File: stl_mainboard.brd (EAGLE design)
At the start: 148.9 x 80 mm, 47 parts, among them IC1 LM555D, IC2 4017D, IC3 ULN2001AD, Q1 AUIRFR5305, Q2 AUIRFR5305, Q3 AUIRFR5305, Q4 AUIRFR5305, Q5 AUIRFR5305, Q6 AUIRFR5305, Q7 AUIRFR5305

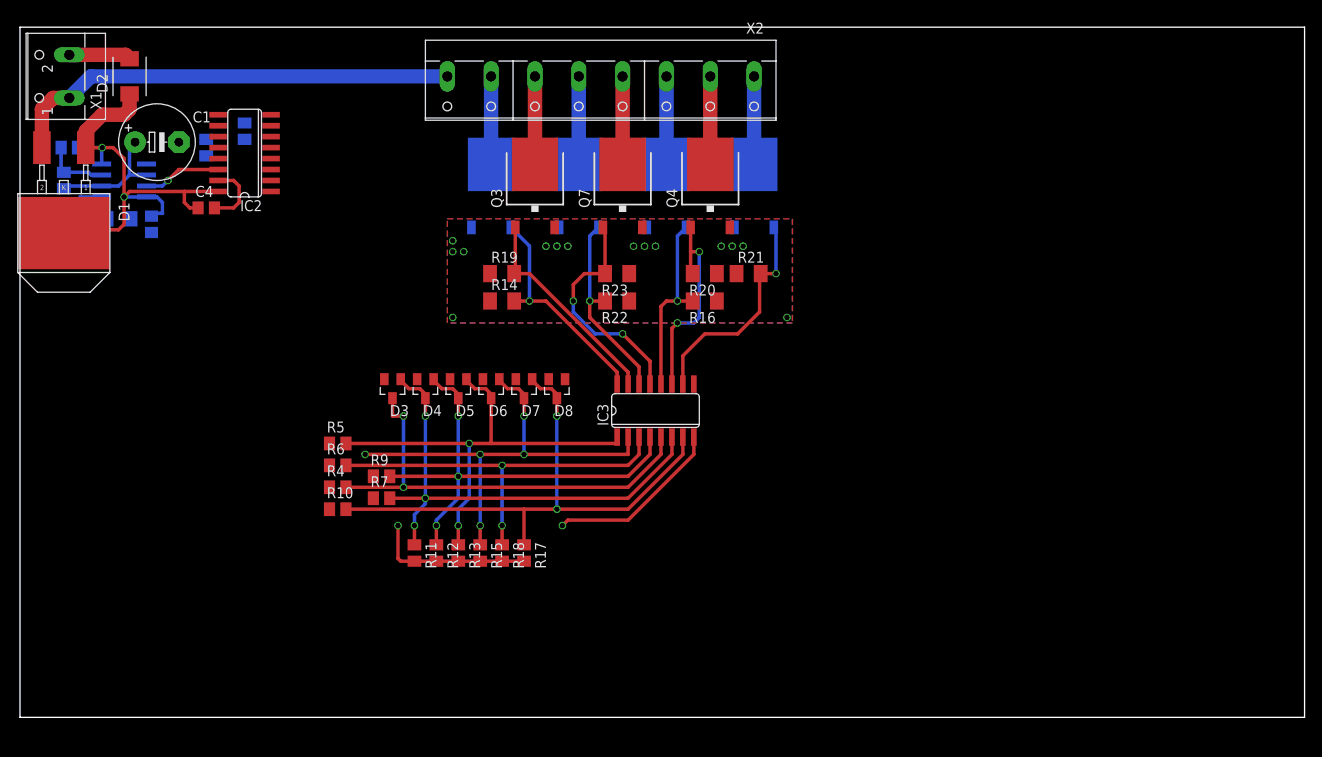
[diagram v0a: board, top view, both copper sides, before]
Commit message: board and schematics done
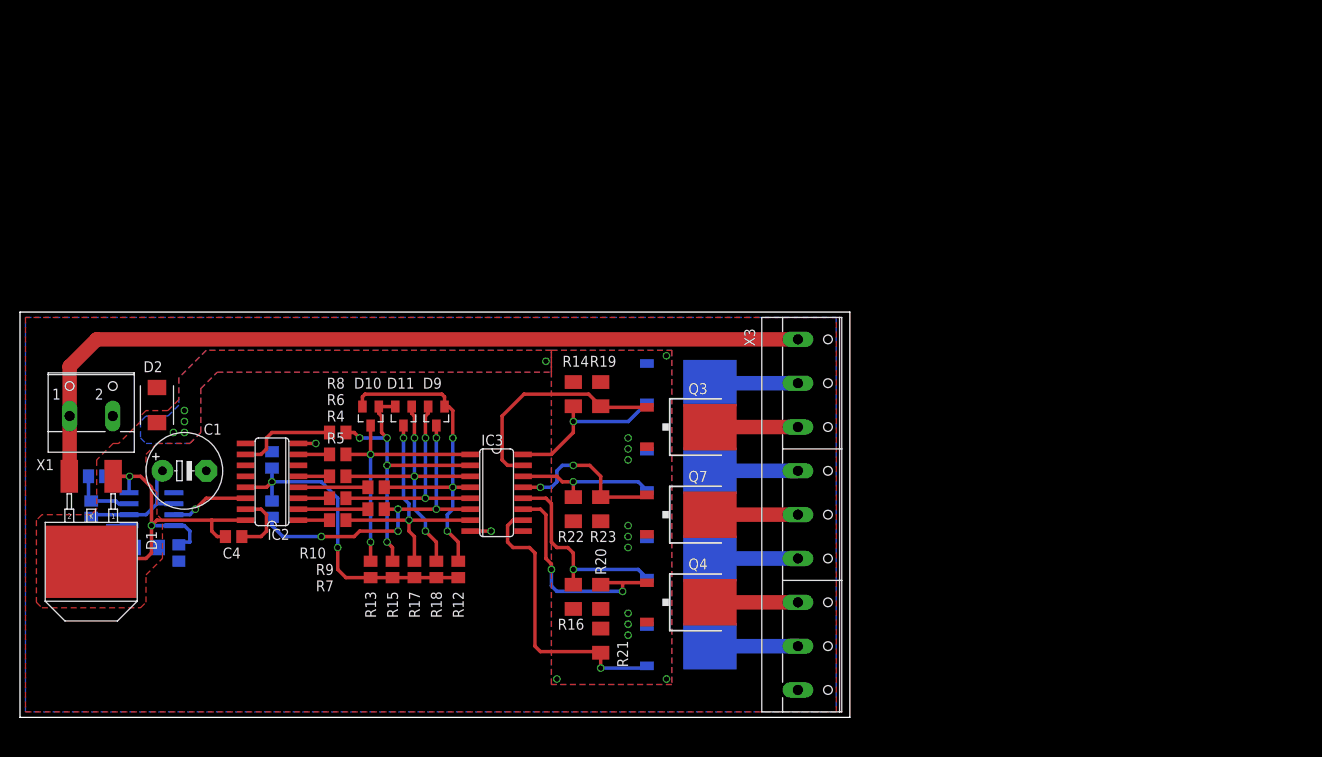
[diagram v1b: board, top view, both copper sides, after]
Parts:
- removed D3, D4, D5, D6, D7, D8: BAS40, diode:SOT23
- removed X2: (no value), con-wago-508:W237-8P
- added D10, D11, D9: BAS40-04, diode:SOT23
- added X3: (no value), con-wago-508:W237-9P
- moved Q5 53.9 mm to (77.5, 8.26), turned to 90 degrees
- moved Q4 48.3 mm to (77.5, 13.3), turned to 270 degrees
- moved R21 45.9 mm to (67.3, 8.89), turned to 270 degrees
- moved Q2 43.3 mm to (77.5, 18.4), turned to 90 degrees
- moved R20 39.4 mm to (67.3, 14.0), turned to 90 degrees
- moved Q7 38.9 mm to (77.5, 23.5), turned to 270 degrees
- moved X1 38.3 mm to (8.26, 36.2), turned to 0 degrees
- moved D1 38.2 mm to (8.26, 27.9)
- moved R2 38.2 mm to (8.89, 27.9)
- moved C4 38.2 mm to (24.8, 21.0)
- moved D2 38.2 mm to (15.9, 36.2)
- moved IC2 38.2 mm to (29.2, 27.3)
- moved C1 38.2 mm to (19.1, 28.6)
- moved C2 38.2 mm to (14.6, 19.7)
- moved C3 38.2 mm to (18.4, 19.1)
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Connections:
- removed net +12V: D1.2, X1.1, X2.8
- new net B+: D1.2, X1.1, X3.1
- net BULB2: now also X3.2; no longer X2.7
- net BULB3: now also X3.3; no longer X2.6
- net BULB4: now also X3.4; no longer X2.5
- net BULB5: now also X3.5; no longer X2.4
- net BULB6: now also X3.6; no longer X2.3
- net BULB7: now also X3.7; no longer X2.2
- net BULB8: now also X3.8; no longer X2.1
- net Q0: now also D9.2; no longer D3.3
- net Q1: now also D9.3; no longer D3.1, D4.3
- net Q2: now also D10.2, D9.1; no longer D4.1, D5.3
- net Q3: now also D10.3; no longer D5.1, D6.3
- net Q4: now also D10.1, D11.2; no longer D6.1, D7.3
- net Q5: now also D11.3; no longer D7.1, D8.3
- net Q6: now also D11.1; no longer D8.1
- net VSS: now also X3.9
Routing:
- net B+: track 0.00 -> 99.1 mm
- net +12V: track 53.0 -> 0.00 mm
- net Q5: track 64.8 -> 30.6 mm
- net Q0: track 51.7 -> 25.1 mm
- net Q3: track 53.8 -> 30.1 mm
- net VSS: track 35.6 -> 12.2 mm, vias 1 -> 2
- net Q1: track 58.5 -> 38.5 mm, vias 3 -> 5
- net CNTR_STOP: track 18.5 -> 38.2 mm, vias 1 -> 2
- net Q4: track 53.6 -> 35.2 mm, vias 5 -> 4
- net Q2: track 55.4 -> 41.4 mm
- net Q6: track 45.7 -> 33.5 mm, vias 2 -> 3
- net N$8: track 0.00 -> 11.5 mm
- net VDD: track 56.3 -> 46.4 mm, vias 16 -> 19
- net N$6: track 0.00 -> 8.04 mm
- net N$5: track 0.00 -> 8.04 mm
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- added copper zone on layer 1, net VSS
- added copper zone on layer 16, net VSS
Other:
- board size 148.9 x 80 mm -> 96.2 x 47 mm

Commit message: improve routing power polygones
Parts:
- moved C2 5.12 mm to (17.1, 15.2)
- moved C3 1.27 mm to (19.7, 19.1)
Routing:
- net VDD: track 46.4 -> 36.4 mm, vias 19 -> 21
- net N$1: track 7.32 -> 14.3 mm
- net B+: track 99.1 -> 99.8 mm
- net VSS: vias 2 -> 6

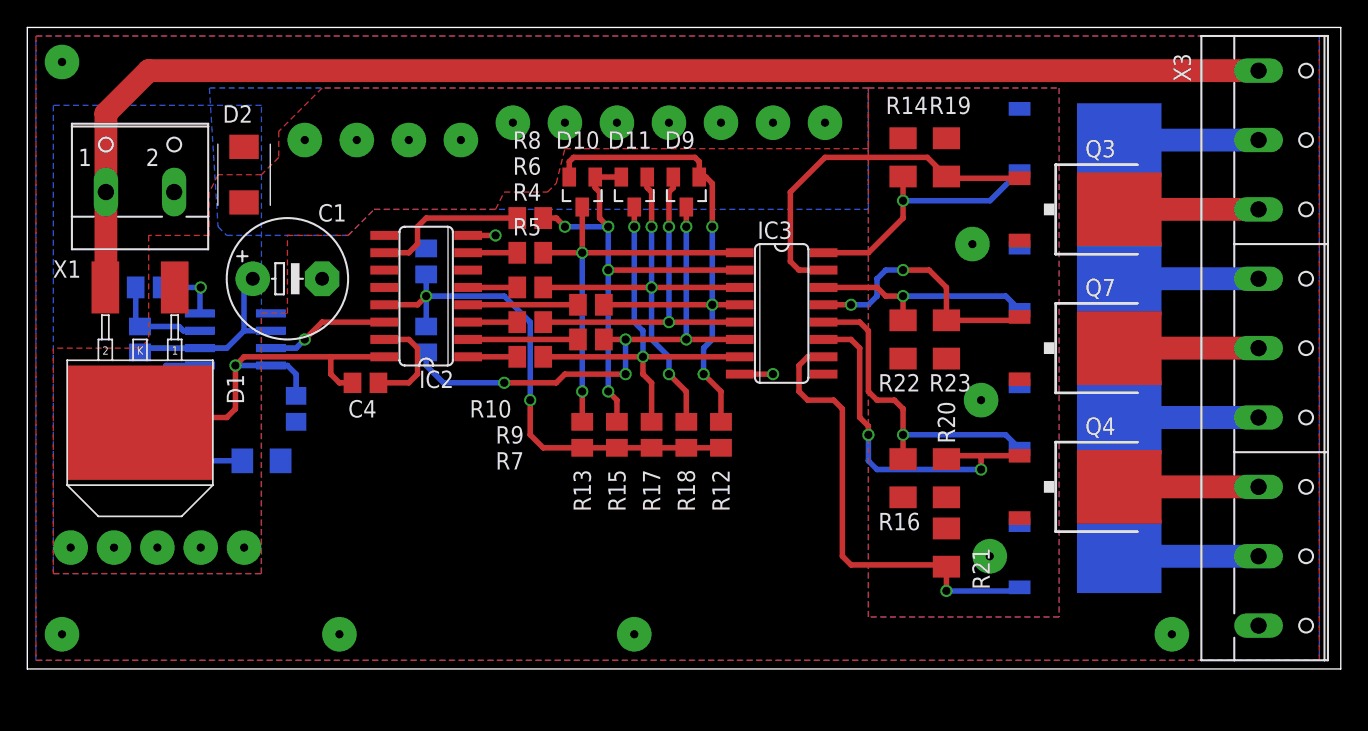
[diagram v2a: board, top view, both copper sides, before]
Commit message: No more 555 and 4017. STM8 instead.
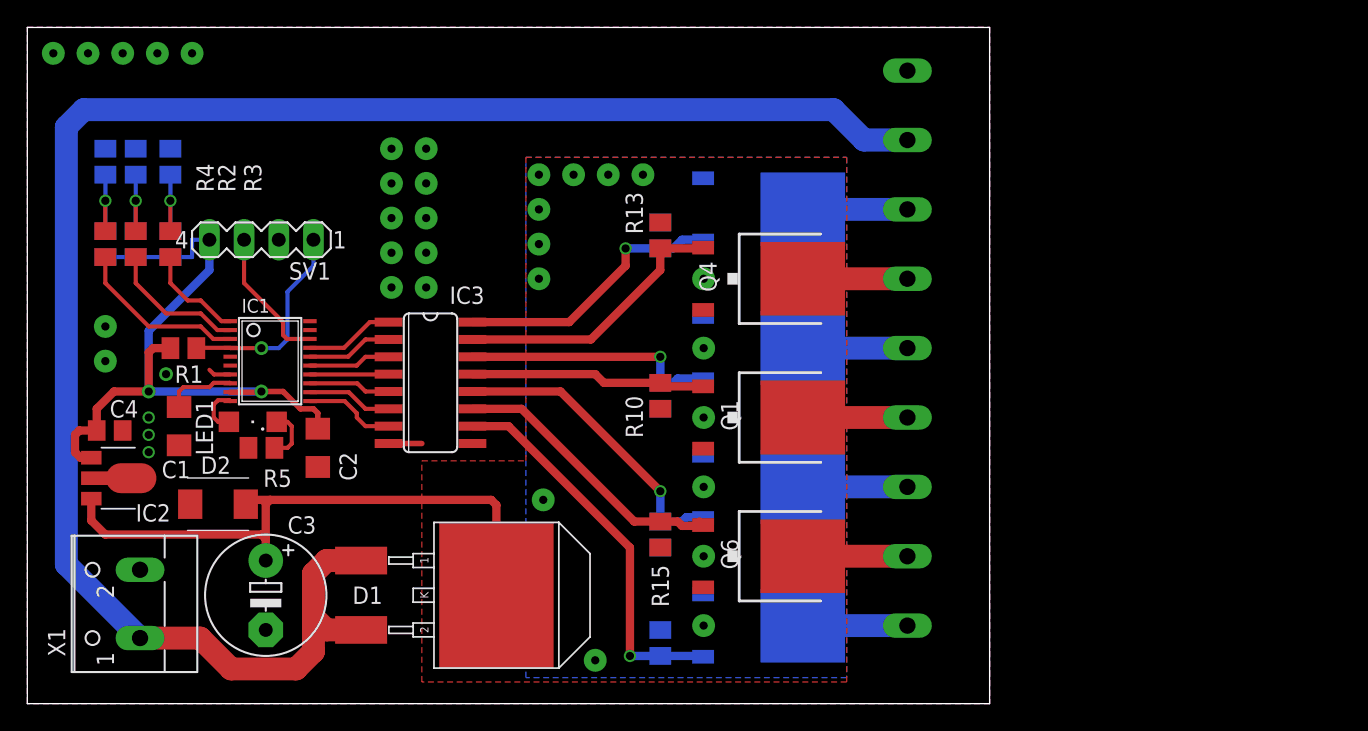
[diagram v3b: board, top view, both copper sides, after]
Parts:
- removed D10, D11, D9: BAS40-04, diode:SOT23
- removed R19, R20, R21, R22, R23: 1K, rcl:M1206
- removed X3: (no value), con-wago-508:W237-9P
- added LED1: (no value), led:SML1206
- added SV1: (no value), con-lstb:MA04-1
- added X2: (no value), con-wago-508:W237-9P
- C1: value 47 -> 1uF; device rcl:E5-8,5 -> rcl:C1206
- C2: value 0.01 -> 100nf
- C3: value 0.1uF -> 0.33; device rcl:C0805 -> rcl:E5-8,5
- C4: value 0.1uF -> 0.1
- D1: value 48CTQ060S -> 48CTQ060; device diode:TO263AB -> 48ctq060:TO263AB
- IC1: value LM555D -> STM8S003F3; device linear:SO08 -> stm8:TSSOP20
- IC2: value 4017D -> 78L05F; device 40xx:SO16 -> linear:SOT89
- R10, R11, R12, R13, R15, R4: value 0 -> 1K
- R14, R16: device rcl:M1206 -> rcl:M0805
- R3: value 4K2 -> 1K
- R5: value 0 -> 5k6
- moved R18 44.8 mm to (5.71, 31.1), flipped to the bottom
- moved R17 40.3 mm to (7.94, 31.1), flipped to the bottom
- moved R7 35.8 mm to (7.94, 37.1), flipped to the bottom, turned to 270 degrees
- moved R6 32.4 mm to (5.71, 37.1), flipped to the bottom, turned to 270 degrees
- moved R4 31.6 mm to (5.71, 31.1), turned to 90 degrees
- moved X1 31.5 mm to (6.99, 4.76), turned to 90 degrees
- moved R9 31.1 mm to (10.5, 31.1), flipped to the bottom, turned to 270 degrees
- moved Q1 30.8 mm to (54.3, 18.4), flipped to the top, turned to 270 degrees
- moved Q3 30.8 mm to (54.3, 13.3), flipped to the bottom, turned to 90 degrees
- moved Q6 30.8 mm to (54.3, 8.26), flipped to the top, turned to 270 degrees
- moved Q7 30.8 mm to (54.3, 3.17), flipped to the bottom, turned to 90 degrees
- moved D1 27.8 mm to (24.4, 5.40), turned to 270 degrees
- moved Q2 27.7 mm to (54.3, 33.7)
- moved Q4 27.7 mm to (54.3, 28.6)
- moved Q5 27.7 mm to (54.3, 23.5)
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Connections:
- removed net BULB2: Q1.3, X3.2
- removed net BULB2_CTRL: IC3.16, Q1.1, R14.2
- removed net BULB3: Q3.3, X3.3
- removed net BULB3_CTRL: IC3.15, Q3.1, R19.2
- removed net BULB4: Q6.3, X3.4
- removed net BULB4_CTRL: IC3.14, Q6.1, R22.2
- removed net BULB5: Q7.3, X3.5
- removed net BULB5_CTRL: IC3.13, Q7.1, R23.2
- removed net BULB6: Q2.3, X3.6
- removed net BULB6_CTRL: IC3.12, Q2.1, R16.2
- removed net BULB7: Q4.3, X3.7
- removed net BULB7_CTRL: IC3.11, Q4.1, R20.2
- removed net BULB8: Q5.3, X3.8
- removed net BULB8_CTRL: IC3.10, Q5.1, R21.2
- removed net CNTR_STOP: IC2.13, R1.1, R11.2, R12.2, R13.2, R15.2, R17.2, R18.2
- removed net N$4: IC2.3, R4.1
- removed net Q0: D9.2, IC3.5, R4.2
- removed net Q1: D9.3, IC3.6, R11.1, R7.2
- removed net Q2: D10.2, D9.1, IC3.4, R12.1, R9.2
- removed net Q3: D10.3, IC3.1, R13.1, R5.2
- removed net Q4: D10.1, D11.2, IC3.2, R15.1, R8.2
- removed net Q5: D11.3, IC3.7, R10.2, R17.1
- removed net Q6: D11.1, IC3.3, R18.1, R6.2
- removed net TMR_OUT: IC1.3, IC2.14
- removed net VSS: C1.-, C2.2, C3.2, C4.2, D2.A, IC1.1, IC2.15, IC2.8, IC3.8, R1.2, X1.2, X3.9
- new net +5V: C2.1, C4.1, IC1.9, IC2.1, R1.1, R17.2, R18.2, R9.2, SV1.4
- new net BULB01: Q2.3, X2.7
- new net BULB01_CTRL: IC3.16, Q2.1, R11.2
- new net BULB02: Q4.3, X2.6
- new net BULB02_CTRL: IC3.15, Q4.1, R13.2
- new net BULB03: Q5.3, X2.5
- new net BULB03_CTRL: IC3.14, Q5.1, R14.2
- new net BULB04: Q1.3, X2.4
- new net BULB04_CTRL: IC3.13, Q1.1, R10.2
- new net BULB05: Q3.3, X2.3
- new net BULB05_CTRL: IC3.12, Q3.1, R12.2
- new net BULB06: Q6.3, X2.2
- new net BULB06_CTRL: IC3.11, Q6.1, R15.2
- new net BULB07: Q7.3, X2.1
- new net BULB07_CTRL: IC3.10, Q7.1, R16.2
- new net GND: C1.2, C2.2, C3.-, C4.2, D2.A, IC1.7, IC2.2, IC2.2@1, IC3.8, R5.2, R6.1, R7.1, R8.1, SV1.2, X1.2, X2.9
- new net NRST: IC1.4, R1.2, SV1.1
- new net Q01: IC1.17, IC3.1
- new net Q02: IC1.16, IC3.2
- new net Q03: IC1.15, IC3.3
- new net Q04: IC1.14, IC3.4
- new net Q05: IC1.13, IC3.5
- new net Q06: IC1.12, IC3.6
- new net Q07: IC1.11, IC3.7
- new net SWIM: IC1.18, SV1.3
- net B+: now also D1.1, X2.8; no longer X3.1
- net N$1: now also IC1.10, LED1.A; no longer C2.1, IC1.5
- net N$10: now also R18.1, R4.2, R6.2; no longer IC2.5, R6.1
- net N$2: now also LED1.C, R5.1; no longer IC1.7, R2.1, R3.1
- net N$3: now also C1.1, IC1.8; no longer C1.+, IC1.2, IC1.6, R3.2
- net N$5: now also IC1.1, R3.1; no longer IC2.2, R7.1
- net N$6: now also IC1.2, R2.1; no longer IC2.4, R9.1
- net N$7: now also IC1.3, R4.1; no longer IC2.7, R5.1
- net N$8: now also R3.2, R8.2, R9.1; no longer IC2.10, R8.1
- net N$9: now also R17.1, R2.2, R7.2; no longer IC2.1, R10.1
- net VDD: now also C3.+, IC2.3, R10.1, R11.1, R12.1, R13.1, R15.1; no longer C3.1, C4.1, D1.1, IC1.4, IC1.8, IC2.16, R19.1, R2.2, R20.1, R21.1, R22.1, R23.1
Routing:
- net +5V: track 0.00 -> 53.2 mm, vias 0 -> 2
- net Q2: track 41.4 -> 0.00 mm, vias 3 -> 0
- net Q1: track 38.5 -> 0.00 mm, vias 5 -> 0
- net CNTR_STOP: track 38.2 -> 0.00 mm, vias 2 -> 0
- net Q4: track 35.2 -> 0.00 mm, vias 4 -> 0
- net BULB8_CTRL: track 33.6 -> 0.00 mm, vias 1 -> 0
- net Q6: track 33.5 -> 0.00 mm, vias 3 -> 0
- net Q5: track 30.6 -> 0.00 mm, vias 2 -> 0
- net B+: track 99.8 -> 130.4 mm
- net Q3: track 30.1 -> 0.00 mm, vias 2 -> 0
- net BULB07_CTRL: track 0.00 -> 28.5 mm, vias 0 -> 1
- net BULB7_CTRL: track 26.4 -> 0.00 mm, vias 2 -> 0
- net BULB3_CTRL: track 26.3 -> 0.00 mm
- net Q0: track 25.1 -> 0.00 mm, vias 2 -> 0
- net BULB6_CTRL: track 23.7 -> 0.00 mm, vias 1 -> 0
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- added copper zone on layer 1, net GND
- added copper zone on layer 16, net GND
- removed copper zone on layer 1, net VSS
- removed copper zone on layer 16, net VSS
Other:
- board size 96.2 x 47 mm -> 70.5 x 49.5 mm

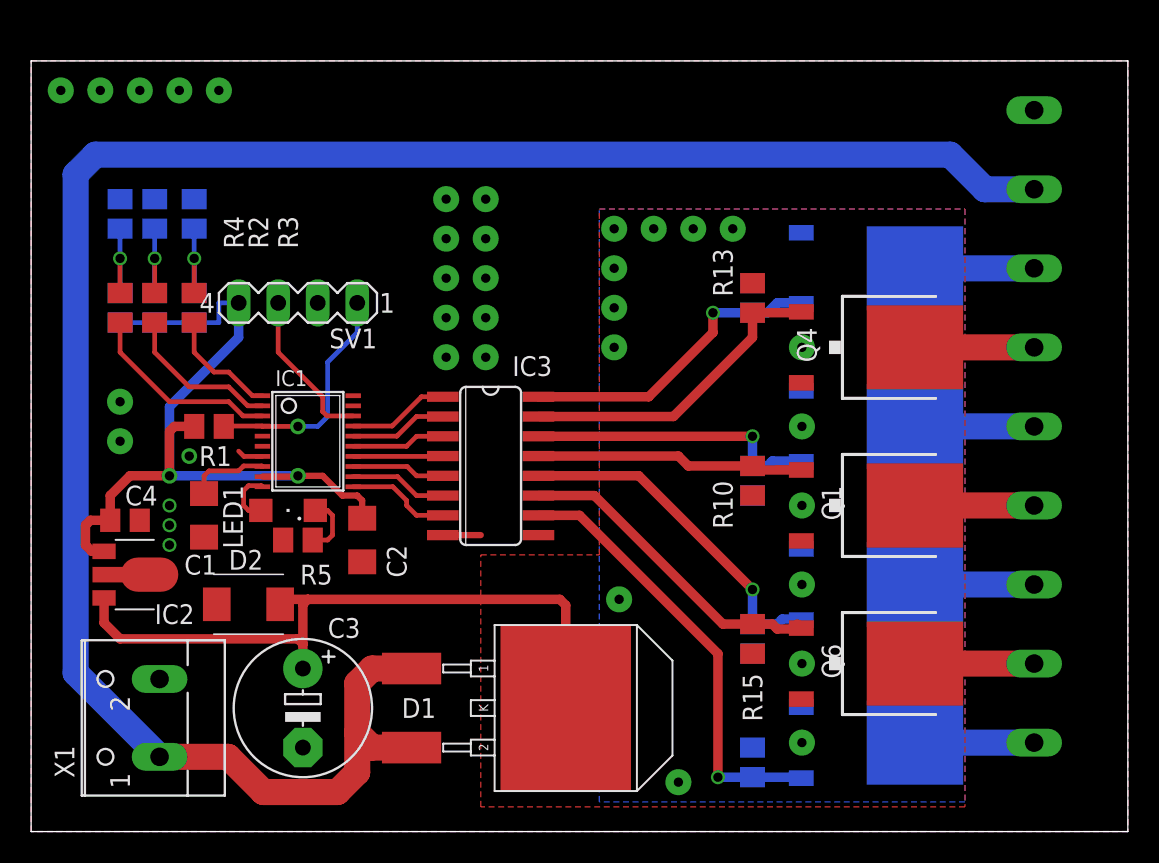
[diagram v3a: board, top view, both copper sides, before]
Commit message: Added 'LEARN' jumper
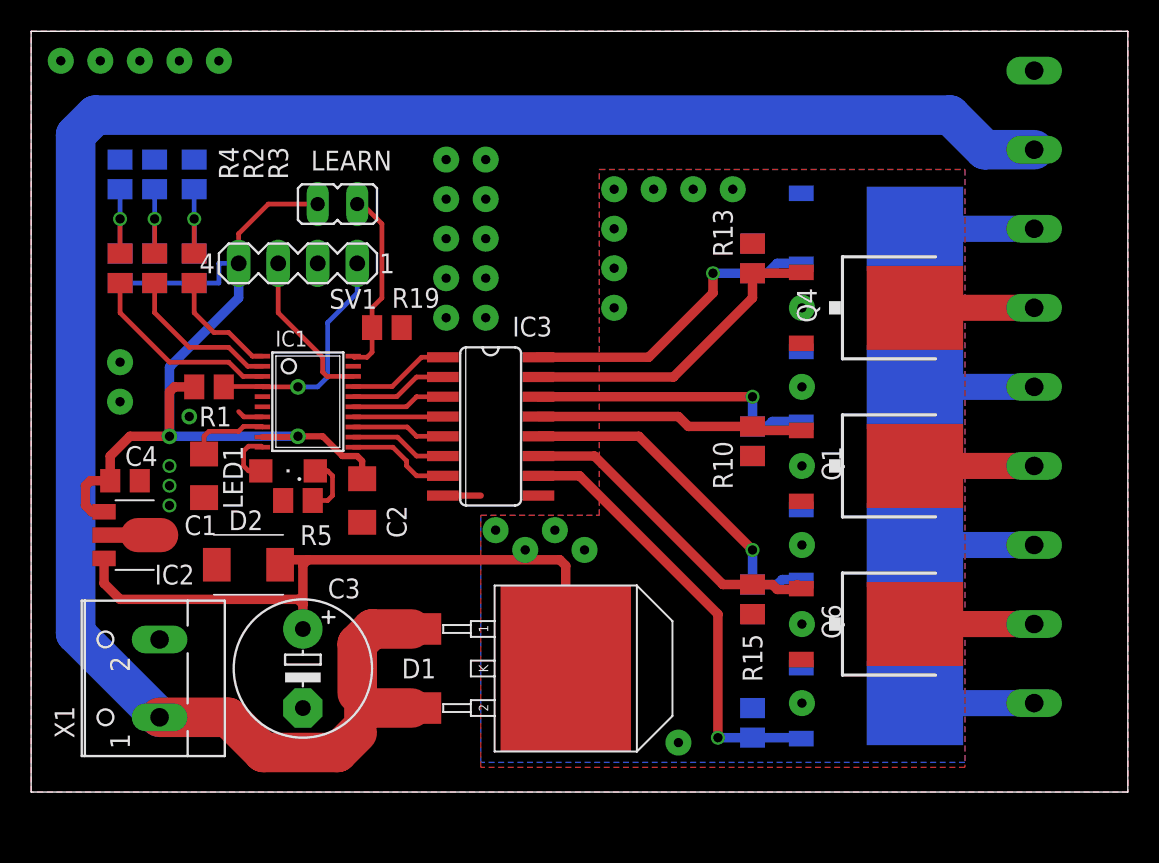
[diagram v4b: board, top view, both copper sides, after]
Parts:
- added LEARN: (no value), jumper:JP1
- added R19: 1K, rcl:M0805
- moved C2 2.54 mm to (21.3, 18.7)
- moved C4 2.54 mm to (6.03, 20.0)
- moved IC3 2.54 mm to (29.5, 23.5)
- moved R17 2.54 mm to (7.94, 33.7)
- moved R18 2.54 mm to (5.71, 33.7)
- moved R2 2.54 mm to (7.94, 33.7)
- moved R3 2.54 mm to (10.5, 33.7)
- moved R4 2.54 mm to (5.71, 33.7)
- moved R5 2.54 mm to (17.1, 18.7)
- moved R9 2.54 mm to (10.5, 33.7)
- moved D2 2.54 mm to (14.0, 14.6)
- moved IC2 2.54 mm to (6.67, 16.5)
- moved R12 2.54 mm to (46.4, 12.4)
- moved R15 2.54 mm to (46.4, 12.4)
- moved C3 2.54 mm to (17.5, 7.94)
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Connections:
- new net LEARN: IC1.20, LEARN.1, R19.2
- net +5V: now also LEARN.2
- net GND: now also R19.1
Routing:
- net LEARN: track 0.00 -> 12.0 mm
- net +5V: track 53.2 -> 61.0 mm
- net VDD: vias 15 -> 18
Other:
- board size 70.5 x 49.5 mm -> 70.5 x 48.9 mm
